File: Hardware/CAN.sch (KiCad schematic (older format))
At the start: 7 parts, among them U2 SN65HVD230

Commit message: Update components for assembly, generate gerbers
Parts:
- R4: Field5 (none) -> 60.4Ω ±1% ±200ppm/℃ 1/16W 0402 Chip Resistor - Surface Moun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; LCSC (none) -> C60310
- R5: Comments (none) -> 60.4Ω ±1% ±200ppm/℃ 1/16W 0402 Chip Resistor - Surface Moun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; LCSC (none) -> C60310
- U2: Comments (none) -> Transceiver 1/1 CAN 1Mbps SOIC-8_150mil CAN ICs ROHS; LCSC (none) -> C12084
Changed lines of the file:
@@
 F 2 "Package_SO:SOIC-8_3.9x4.9mm_P1.27mm" H 5370 3450 50  0001 C CNN
 F 3 "http://www.ti.com/lit/ds/symlink/sn65hvd230.pdf" H 5270 4350 50  0001 C CNN
+F 4 "C12084" H 5370 3950 50  0001 C CNN "LCSC"
+F 5 "Transceiver 1/1 CAN 1Mbps SOIC-8_150mil CAN ICs ROHS" H 5370 3950 50  0001 C CNN "Comments"
 	1    5370 3950
 	1    0    0    -1
@@
 F 2 "Resistor_SMD:R_0402_1005Metric" V 6810 4340 50  0001 C CNN
 F 3 "~" H 6770 4350 50  0001 C CNN
+F 4 "C60310" H 6770 4350 50  0001 C CNN "LCSC"
+F 5 "60.4Ω ±1% ±200ppm/℃ 1/16W 0402 Chip Resistor - Surface Mount ROHS" H 6770 4350 50  0001 C CNN "Comments"
 	1    6770 4350
 	1    0    0    -1
@@
 F 2 "Resistor_SMD:R_0402_1005Metric" V 6810 3690 50  0001 C CNN
 F 3 "~" H 6770 3700 50  0001 C CNN
+F 4 "C60310" H 6770 3700 50  0001 C CNN "LCSC"
+F 5 "60.4Ω ±1% ±200ppm/℃ 1/16W 0402 Chip Resistor - Surface Mount ROHS" H 6770 3700 50  0001 C CNN "Field5"
 	1    6770 3700
 	1    0    0    -1

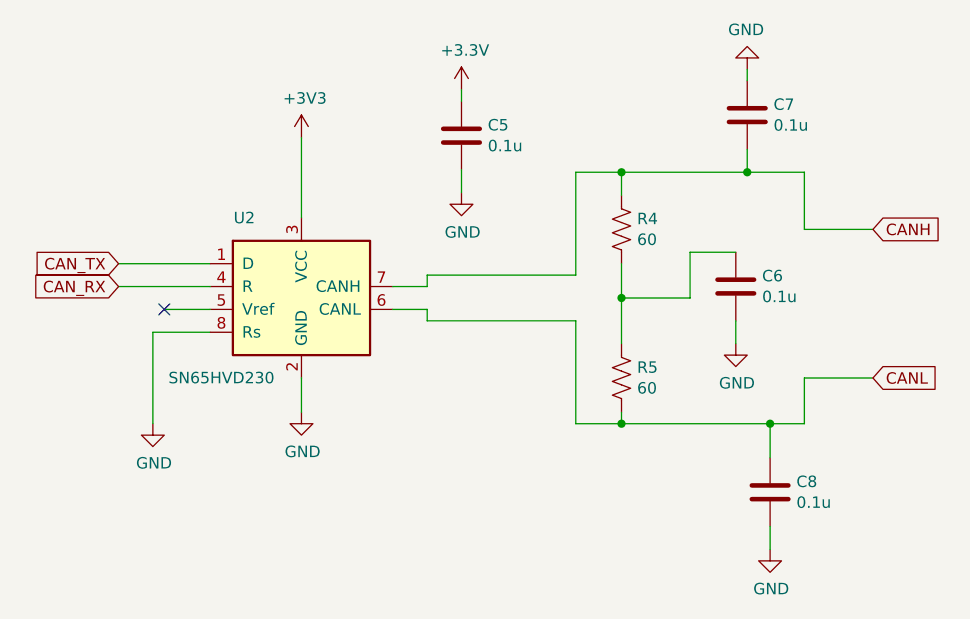
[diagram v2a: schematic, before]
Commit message: Update board layout
Fix OLED pads to meet intended design. Move all non UI components to one side of the board for better single sided assembly.
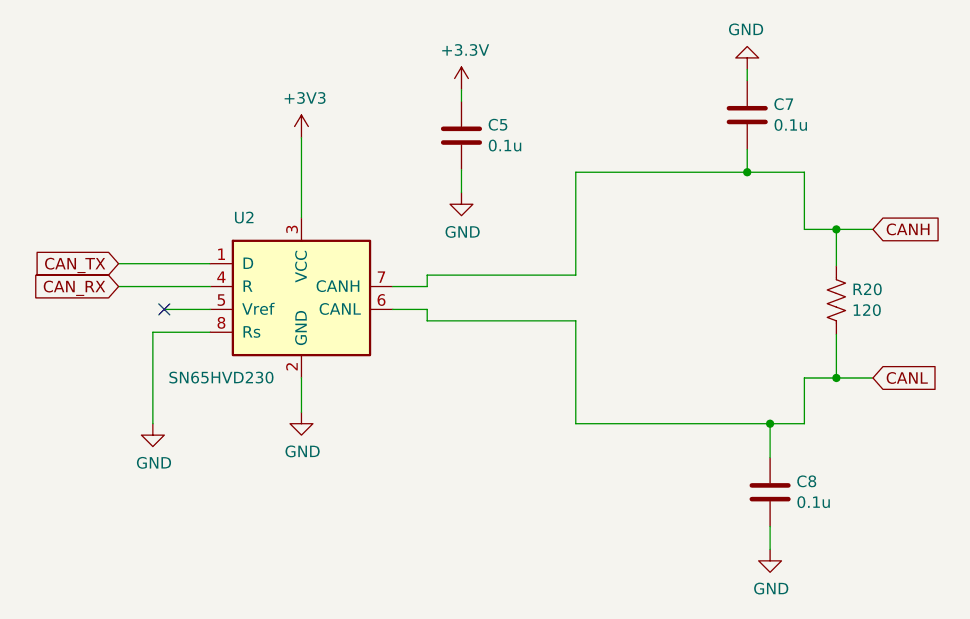
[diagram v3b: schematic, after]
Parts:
- removed C6: 0.1u, Capacitor_SMD:C_0402_1005Metric, symbol Device:C
- removed R4, R5: 60, Resistor_SMD:R_0402_1005Metric, symbol Device:R_US
- added R20: 120, Resistor_SMD:R_0402_1005Metric, symbol Device:R_US
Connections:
- net CANH: now also R20.1
- net CANL: now also R20.2
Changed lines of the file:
@@
 	7320 3350 7320 3450
-Wire Wire Line
-	7320 3050 7320 3000
 Wire Wire Line
 	7420 5000 7420 5100
@@
 	1    7420 5100
 	1    0    0    -1
-$EndComp
-$Comp
-L power:GND #PWR0136
-U 1 1 61436113
-P 7320 3000
-F 0 "#PWR0136" H 7320 2750 50  0001 C CNN
-F 1 "GND" H 7325 2827 50  0000 C CNN
-F 2 "" H 7320 3000 50  0001 C CNN
-F 3 "" H 7320 3000 50  0001 C CNN
-	1    7320 3000
-	-1   0    0    1
 $EndComp
 Wire Wire Line
@@
 	1    0    0    -1
 $EndComp
-$Comp
-L Device:C C7
-U 1 1 613E53B9
-P 7320 3200
-F 0 "C7" H 7435 3246 50  0000 L CNN
-F 1 "0.1u" H 7435 3155 50  0000 L CNN
-F 2 "Capacitor_SMD:C_0402_1005Metric" H 7358 3050 50  0001 C CNN
-F 3 "~" H 7320 3200 50  0001 C CNN
-	1    7320 3200
-	1    0    0    -1
-$EndComp
 Wire Wire Line
-	7570 4350 7870 4350
+	7570 4350 7710 4350
 Wire Wire Line
-	7570 3700 7870 3700
+	7570 3700 7710 3700
 Wire Wire Line
 	7570 3450 7570 3700
@@
 Wire Wire Line
 	6570 3900 6570 3450
-Wire Wire Line
-	6770 4550 7420 4550
-Wire Wire Line
-	6570 4550 6770 4550
-Connection ~ 6770 4550
-Wire Wire Line
-	6770 4550 6770 4500
-Wire Wire Line
-	6770 3450 7320 3450
-Wire Wire Line
-	6570 3450 6770 3450
-Connection ~ 6770 3450
-Wire Wire Line
-	6770 3450 6770 3550
-$Comp
-L Device:R_US R5
-U 1 1 6137B5AC
-P 6770 4350
-F 0 "R5" H 6838 4396 50  0000 L CNN
-F 1 "60" H 6838 4305 50  0000 L CNN
-F 2 "Resistor_SMD:R_0402_1005Metric" V 6810 4340 50  0001 C CNN
-F 3 "~" H 6770 4350 50  0001 C CNN
-F 4 "C60310" H 6770 4350 50  0001 C CNN "LCSC"
-F 5 "60.4Ω ±1% ±200ppm/℃ 1/16W 0402 Chip Resistor - Surface Mount ROHS" H 6770 4350 50  0001 C CNN "Comments"
-	1    6770 4350
-	1    0    0    -1
-$EndComp
-$Comp
-L Device:R_US R4
-U 1 1 61379F14
-P 6770 3700
-F 0 "R4" H 6838 3746 50  0000 L CNN
-F 1 "60" H 6838 3655 50  0000 L CNN
-F 2 "Resistor_SMD:R_0402_1005Metric" V 6810 3690 50  0001 C CNN
-F 3 "~" H 6770 3700 50  0001 C CNN
-F 4 "C60310" H 6770 3700 50  0001 C CNN "LCSC"
-F 5 "60.4Ω ±1% ±200ppm/℃ 1/16W 0402 Chip Resistor - Surface Mount ROHS" H 6770 3700 50  0001 C CNN "Field5"
-	1    6770 3700
-	1    0    0    -1
-$EndComp
-Wire Wire Line
-	7070 4000 7070 3800
-Wire Wire Line
-	6770 4000 6770 4200
-Wire Wire Line
-	6770 3850 6770 4000
-Connection ~ 6770 4000
-Wire Wire Line
-	6770 4000 7070 4000
-Wire Wire Line
-	7070 3800 7270 3800
-Wire Wire Line
-	7270 4100 7270 4200
-$Comp
-L power:GND #PWR0139
-U 1 1 6139F007
-P 7270 4200
-F 0 "#PWR0139" H 7270 3950 50  0001 C CNN
-F 1 "GND" H 7275 4027 50  0000 C CNN
-F 2 "" H 7270 4200 50  0001 C CNN
-F 3 "" H 7270 4200 50  0001 C CNN
-	1    7270 4200
-	1    0    0    -1
-$EndComp
-$Comp
-L Device:C C6
-U 1 1 6138FF4D
-P 7270 3950
-F 0 "C6" H 7385 3996 50  0000 L CNN
-F 1 "0.1u" H 7385 3905 50  0000 L CNN
-F 2 "Capacitor_SMD:C_0402_1005Metric" H 7308 3800 50  0001 C CNN
-F 3 "~" H 7270 3950 50  0001 C CNN
-	1    7270 3950
-	1    0    0    -1
-$EndComp
 Wire Wire Line
 	5920 3900 6570 3900
@@
 Text GLabel 7870 3700 2    50   Input ~ 0
 CANH
+$Comp
+L Device:R_US R20
+U 1 1 61AD9622
+P 7710 4010
+F 0 "R20" H 7778 4056 50  0000 L CNN
+F 1 "120" H 7778 3965 50  0000 L CNN
+F 2 "Resistor_SMD:R_0402_1005Metric" V 7750 4000 50  0001 C CNN
+F 3 "~" H 7710 4010 50  0001 C CNN
+F 4 "C60310" H 7710 4010 50  0001 C CNN "LCSC"
+F 5 "60.4Ω ±1% ±200ppm/℃ 1/16W 0402 Chip Resistor - Surface Mount ROHS" H 7710 4010 50  0001 C CNN "Field5"
+	1    7710 4010
+	1    0    0    -1
+$EndComp
+Wire Wire Line
+	7710 3860 7710 3700
+Connection ~ 7710 3700
+Wire Wire Line
+	7710 3700 7870 3700
+Wire Wire Line
+	7710 4160 7710 4350
+Connection ~ 7710 4350
+Wire Wire Line
+	7710 4350 7870 4350
+$Comp
+L Device:C C7
+U 1 1 613E53B9
+P 7320 3200
+F 0 "C7" H 7435 3246 50  0000 L CNN
+F 1 "0.1u" H 7435 3155 50  0000 L CNN
+F 2 "Capacitor_SMD:C_0402_1005Metric" H 7358 3050 50  0001 C CNN
+F 3 "~" H 7320 3200 50  0001 C CNN
+	1    7320 3200
+	1    0    0    -1
+$EndComp
+$Comp
+L power:GND #PWR0136
+U 1 1 61436113
+P 7320 3000
+F 0 "#PWR0136" H 7320 2750 50  0001 C CNN
+F 1 "GND" H 7325 2827 50  0000 C CNN
+F 2 "" H 7320 3000 50  0001 C CNN
+F 3 "" H 7320 3000 50  0001 C CNN
+	1    7320 3000
+	-1   0    0    1
+$EndComp
+Wire Wire Line
+	7320 3050 7320 3000
+Wire Wire Line
+	6570 3450 7320 3450
+Wire Wire Line
+	6570 4550 7420 4550
 $EndSCHEMATC

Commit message: Updates
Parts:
- C7, C8: value 0.1u -> 0
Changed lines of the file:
@@
 Title "CAN Gauge"
 Date "2021-10-10"
-Rev "B"
+Rev "C"
 Comp ""
 Comment1 ""
@@
 P 7420 4850
 F 0 "C8" H 7535 4896 50  0000 L CNN
-F 1 "0.1u" H 7535 4805 50  0000 L CNN
+F 1 "0" H 7535 4805 50  0000 L CNN
 F 2 "Capacitor_SMD:C_0402_1005Metric" H 7458 4700 50  0001 C CNN
 F 3 "~" H 7420 4850 50  0001 C CNN
@@
 P 7320 3200
 F 0 "C7" H 7435 3246 50  0000 L CNN
-F 1 "0.1u" H 7435 3155 50  0000 L CNN
+F 1 "0" H 7435 3155 50  0000 L CNN
 F 2 "Capacitor_SMD:C_0402_1005Metric" H 7358 3050 50  0001 C CNN
 F 3 "~" H 7320 3200 50  0001 C CNN
